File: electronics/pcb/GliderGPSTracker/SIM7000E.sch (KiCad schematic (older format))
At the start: 12 parts

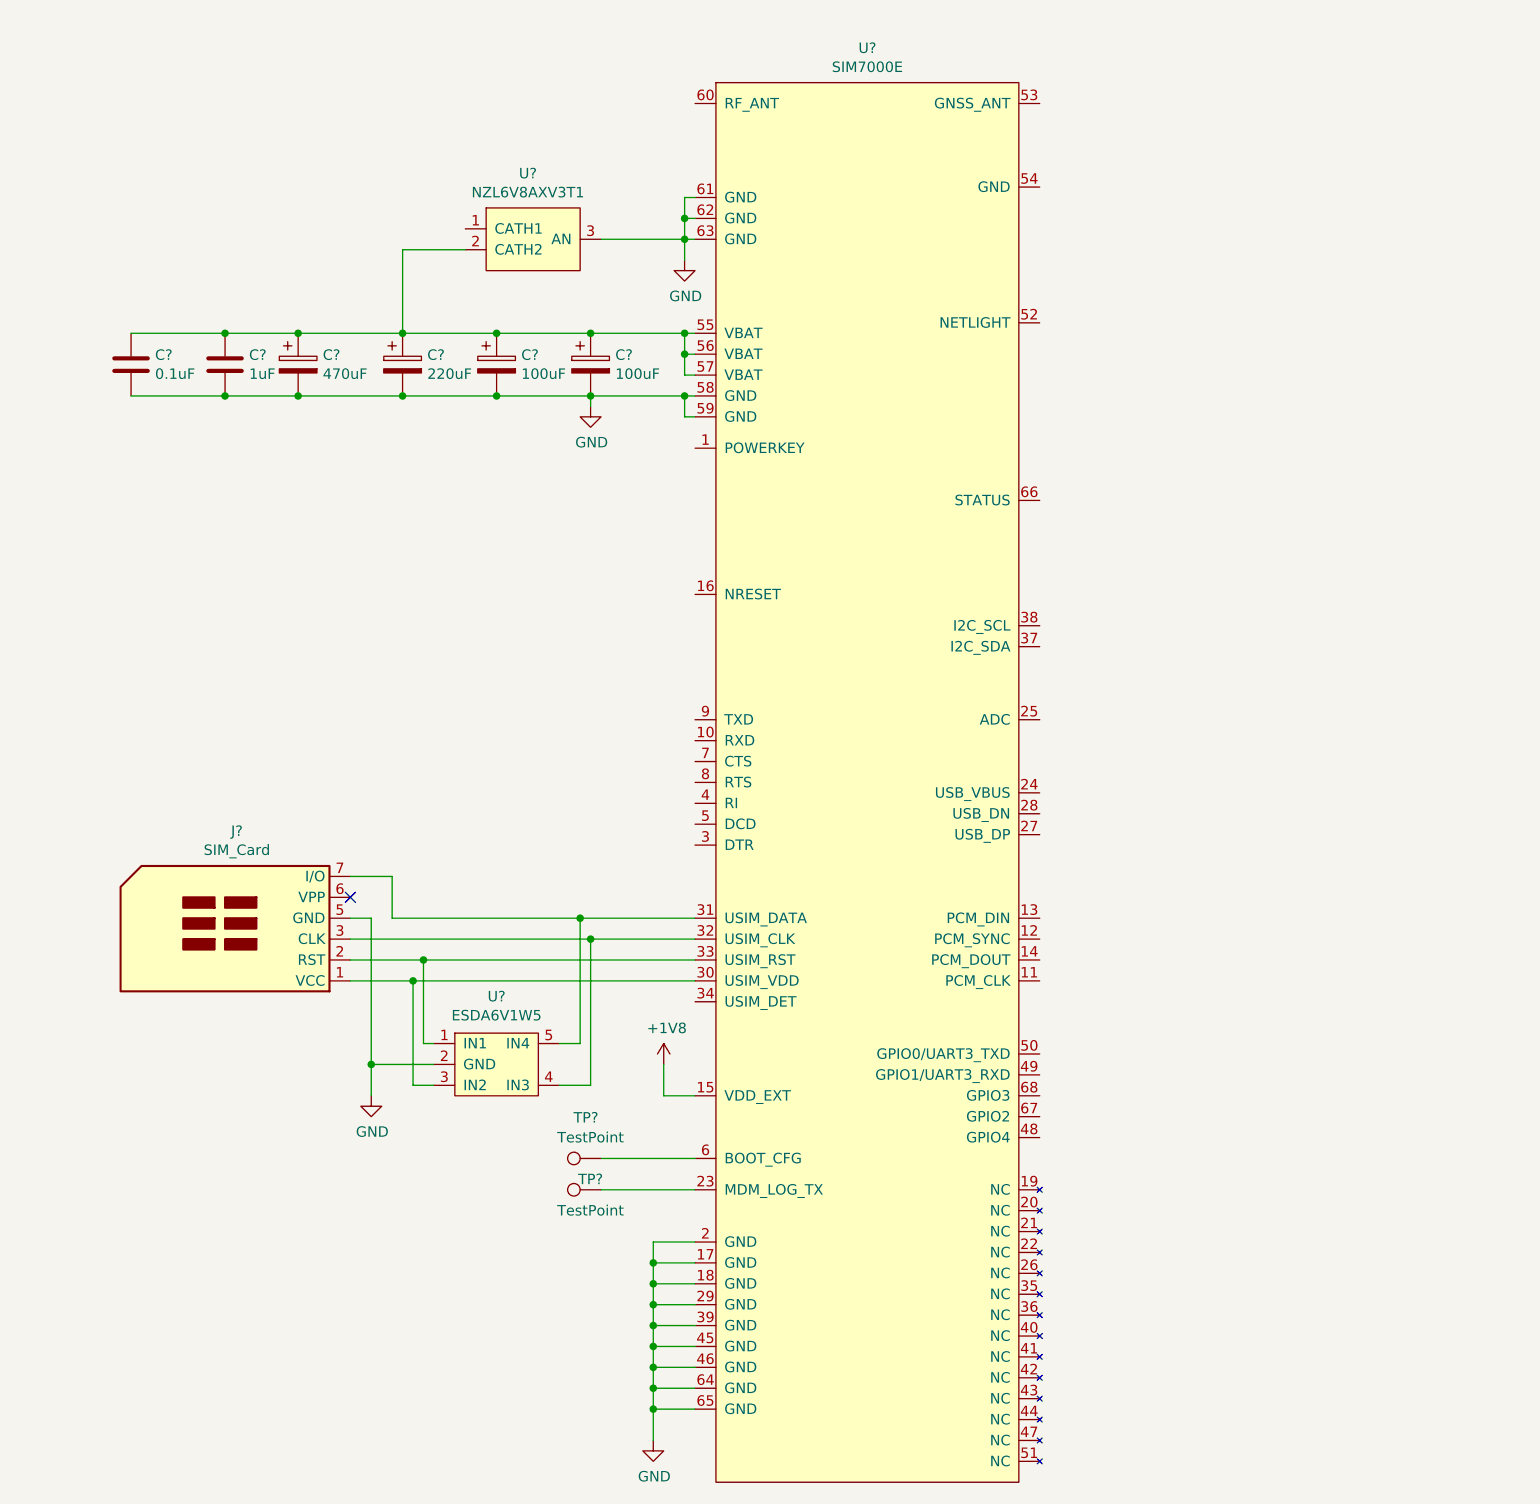
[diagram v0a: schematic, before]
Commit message: Task: SIM7000 Powerkey, reset, USB, UART implementation
The SIM7000 schematic has been updated to include the recommended
layouts for the Powerkey pin, reset pin, USB and UART buses, and
netlight pin. The usb connector in the power schematic has also
been updated to accomodate the additions.
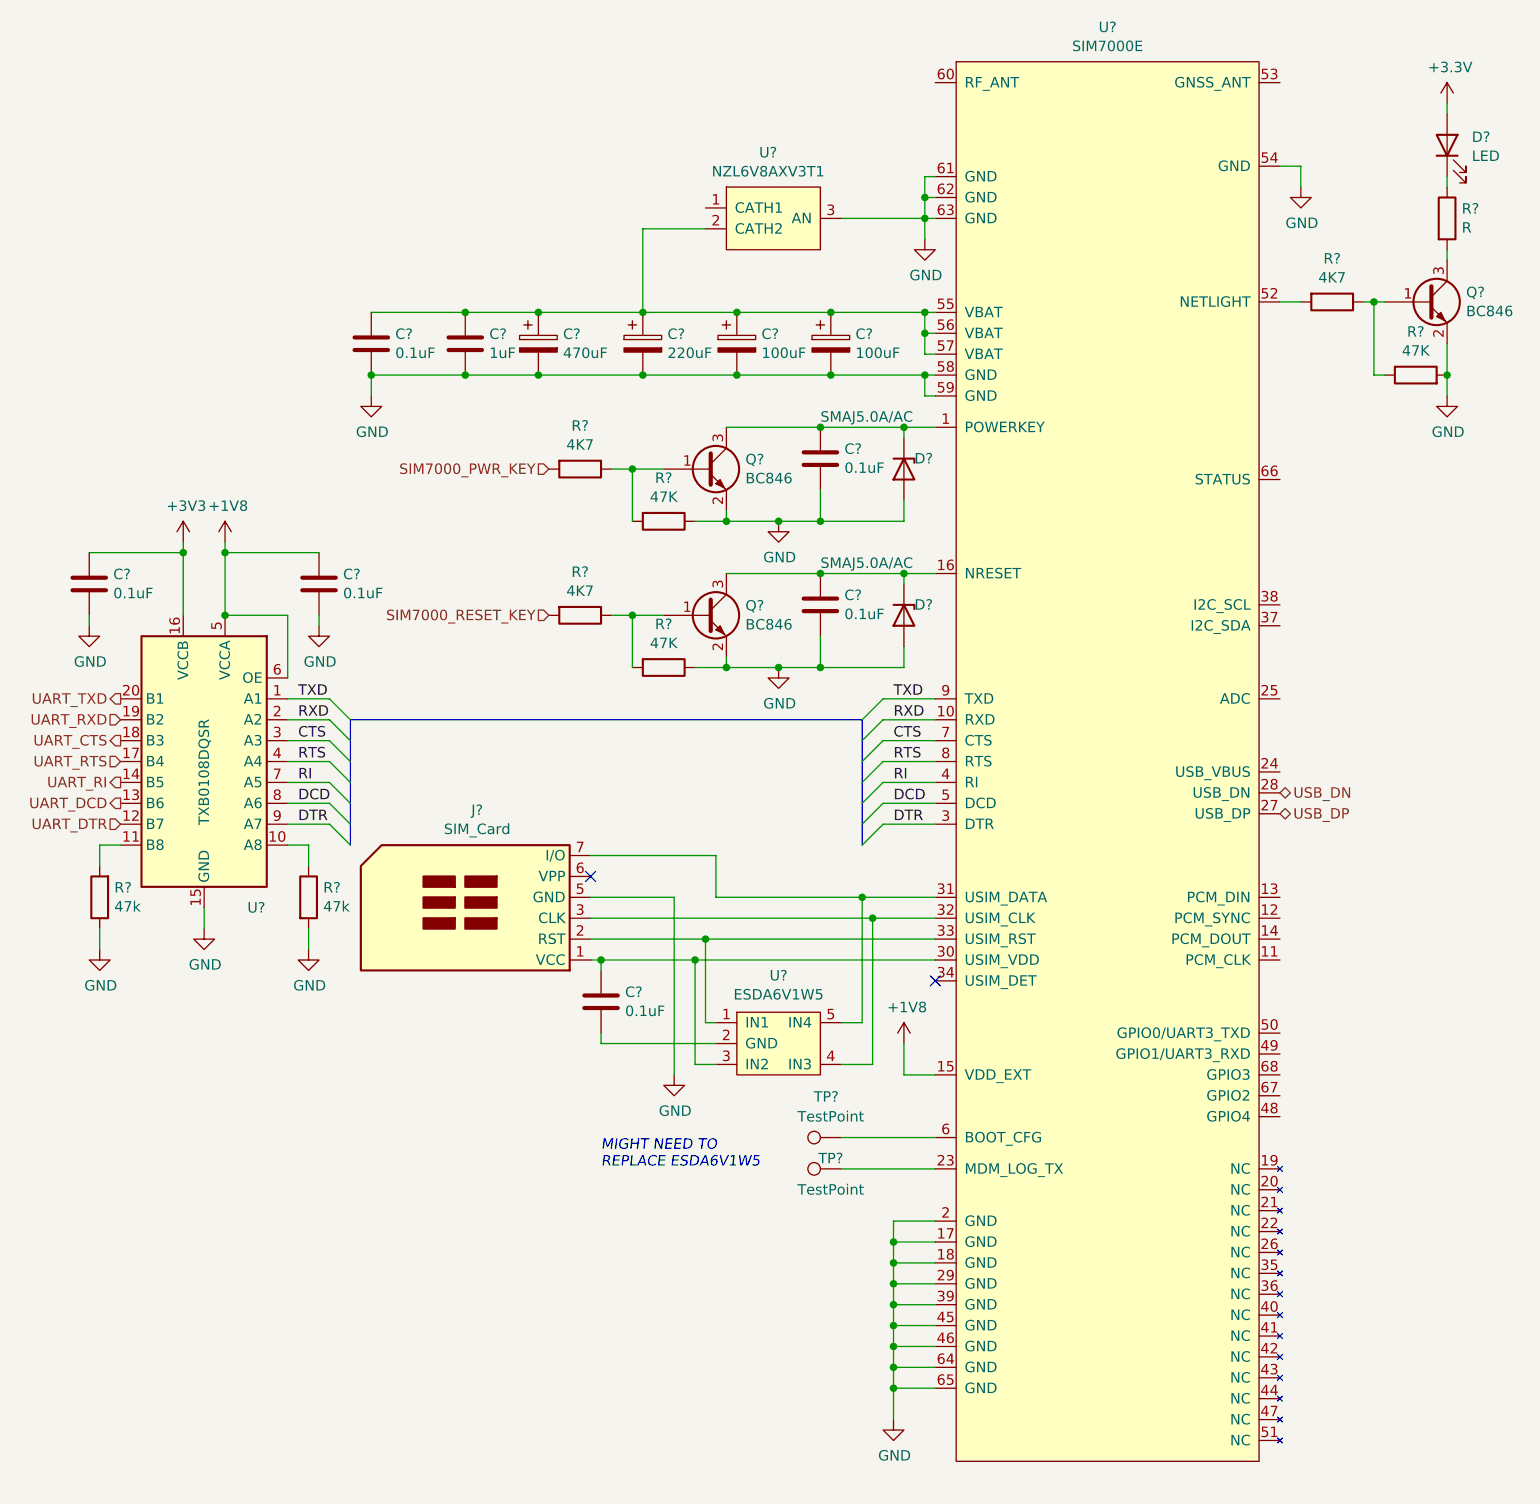
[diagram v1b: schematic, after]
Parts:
- added C? (x5): 0.1uF, symbol Device:C
- added D? (x2): SMAJ5.0A/AC, symbol Device:D_Zener
- added D?: LED, symbol Device:LED
- added Q? (x3): BC846, Package_TO_SOT_SMD:SOT-23, symbol Transistor_BJT:BC846
- added R? (x3): 4K7, symbol Device:R
- added R? (x3): 47K, symbol Device:R
- added R? (x2): 47k, symbol Device:R
- added R?: R, symbol Device:R
- added U?: TXB0108DQSR, Package_SON:USON-20_2x4mm_P0.4mm, symbol Logic_LevelTranslator:TXB0108DQSR
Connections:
- net +1V8: now also C?.1, U?.5 (VCCA), U?.6 (OE)
- net GND: now also U?.54 (GND), C?.2, C?.2, C?.2, C?.2, D?.2 (A), D?.2 (A), Q?.2 (E), Q?.2 (E), Q?.2 (E), R?.1, R?.1, R?.1, R?.2, R?.2, U?.15 (GND); no longer U?.2 (GND)
- net at U?.1 (POWERKEY): now also C?.1, D?.1 (K), Q?.3 (C)
- net RXD: now reaches U?.10 (RXD)
- net RXD: now also U?.2 (A2)
- net at U?.16 (NRESET): now also C?.1, D?.1 (K), Q?.3 (C)
- net USB_DP: now reaches U?.27 (USB_DP)
- net USB_DN: now reaches U?.28 (USB_DN)
- net DTR: now reaches U?.3 (DTR)
- net DTR: now also U?.9 (A7)
- net at J?.1 (VCC), U?.3 (IN2), U?.30 (USIM_VDD): now also C?.1
- net RI: now reaches U?.4 (RI)
- net RI: now also U?.7 (A5)
- net DCD: now reaches U?.5 (DCD)
- net DCD: now also U?.8 (A6)
- net at U?.52 (NETLIGHT): now also R?.2
- net CTS: now reaches U?.7 (CTS)
- net CTS: now also U?.3 (A3)
- net RTS: now reaches U?.8 (RTS)
- net RTS: now also U?.4 (A4)
- net TXD: now reaches U?.9 (TXD)
- net TXD: now also U?.1 (A1)
- new net: C?.2, U?.2 (GND)
- new net: Q?.1 (B), R?.1, R?.2 (x2)
- new net: R?.1, U?.10 (A8)
- new net: R?.2, U?.11 (B8)
- new net: Q?.1 (B), R?.1, R?.1
- new net: Q?.3 (C), R?.2
- new net: D?.1 (K), R?.1
- new net +3V3: C?.1, D?.2 (A), U?.16 (VCCB)
- new net SIM7000_PWR_KEY: R?.2
- new net SIM7000_RESET_KEY: R?.2
- new net UART_CTS: U?.18 (B3)
- new net UART_DCD: U?.13 (B6)
- new net UART_DTR: U?.12 (B7)
- new net UART_RI: U?.14 (B5)
- new net UART_RTS: U?.17 (B4)
- new net UART_RXD: U?.19 (B2)
- new net UART_TXD: U?.20 (B1)
- no-connect marks 1 -> 2
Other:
- note added: "MIGHT NEED TO \nREPLACE ESDA6V1W5\n"
- moved on the sheet: C?, J?, TP?, U?
